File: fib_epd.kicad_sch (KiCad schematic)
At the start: 0 parts

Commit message: restructured EPD side of things, replaced rp2040 with esp32 s3 because of it's LCD controller, USB, LP WIFI_BT & EPDiy compat, repurposed USB0 for ESP interfacing, added e-ink pmic
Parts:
- added U1: TPS651851RSLT, Fibel2:IC_TPS651851, symbol Fibel2:TPS651851RSLT
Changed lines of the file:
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@@
 	(generator_version "8.0")
 	(paper "A4")
+	(symbol
+		(lib_id "Fibel2:TPS651851RSLT")
+		(at 72.39 124.46 0)
+		(unit 1)
+		(exclude_from_sim no)
+		(in_bom yes)
+		(on_board yes)
+		(dnp no)
+		(fields_autoplaced yes)
+		(property "Reference" "U1"
+			(at 72.39 30.48 0)
+			(effects
+				(font
+					(size 1.27 1.27)
+				)
+			)
+		)
+		(property "Value" "TPS651851RSLT"
+			(at 72.39 33.02 0)
+			(effects
+				(font
+					(size 1.27 1.27)
+				)
+			)
+		)
+		(property "Footprint" "Fibel2:IC_TPS651851"
+			(at 73.66 223.266 0)
+			(effects
+				(font
+					(size 1.27 1.27)
+				)
+				(justify bottom)
+				(hide yes)
+			)
+		)
+		(property "Datasheet" ""
+			(at 72.39 124.46 0)
+			(effects
+				(font
+					(size 1.27 1.27)
+				)
+				(hide yes)
+			)
+		)
+		(property "Description" ""
+			(at 72.39 124.46 0)
+			(effects
+				(font
+					(size 1.27 1.27)
+				)
+				(hide yes)
+			)
+		)
+		(property "Package" "VQFN(48)-49 Texas Instruments"
+			(at 73.66 223.266 0)
+			(effects
+				(font
+					(size 1.27 1.27)
+				)
+				(justify bottom)
+				(hide yes)
+			)
+		)
+		(property "MP" "TPS651851RSLT"
+			(at 72.39 124.46 0)
+			(effects
+				(font
+					(size 1.27 1.27)
+				)
+				(justify bottom)
+				(hide yes)
+			)
+		)
+		(pin "5"
+		)
+		(pin "9"
+		)
+		(pin "48"
+		)
+		(pin "19"
+		)
+		(pin "20"
+		)
+		(pin "25"
+		)
+		(pin "16"
+		)
+		(pin "30"
+		)
+		(pin "14"
+		)
+		(pin "24"
+		)
+		(pin "43"
+		)
+		(pin "40"
+		)
+		(pin "12"
+		)
+		(pin "7"
+		)
+		(pin "8"
+		)
+		(pin "10"
+		)
+		(pin "15"
+		)
+		(pin "3"
+		)
+		(pin "18"
+		)
+		(pin "47"
+		)
+		(pin "6"
+		)
+		(pin "39"
+		)
+		(pin "35"
+		)
+		(pin "46"
+		)
+		(pin "36"
+		)
+		(pin "32"
+		)
+		(pin "31"
+		)
+		(pin "27"
+		)
+		(pin "29"
+		)
+		(pin "41"
+		)
+		(pin "13"
+		)
+		(pin "11"
+		)
+		(pin "28"
+		)
+		(pin "38"
+		)
+		(pin "34"
+		)
+		(pin "26"
+		)
+		(pin "4"
+		)
+		(pin "42"
+		)
+		(pin "44"
+		)
+		(pin "45"
+		)
+		(pin "37"
+		)
+		(pin "22"
+		)
+		(pin "17"
+		)
+		(pin "2"
+		)
+		(pin "33"
+		)
+		(pin "1"
+		)
+		(pin "21"
+		)
+		(pin "23"
+		)
+		(instances
+			(project "Fibel2"
+				(path "/862c21e2-7ec9-4f80-a33c-aad02ea9423e/5a179277-42b3-47ed-bc0e-bf53dbccdf92"
+					(reference "U1")
+					(unit 1)
+				)
+			)
+		)
+	)
 )

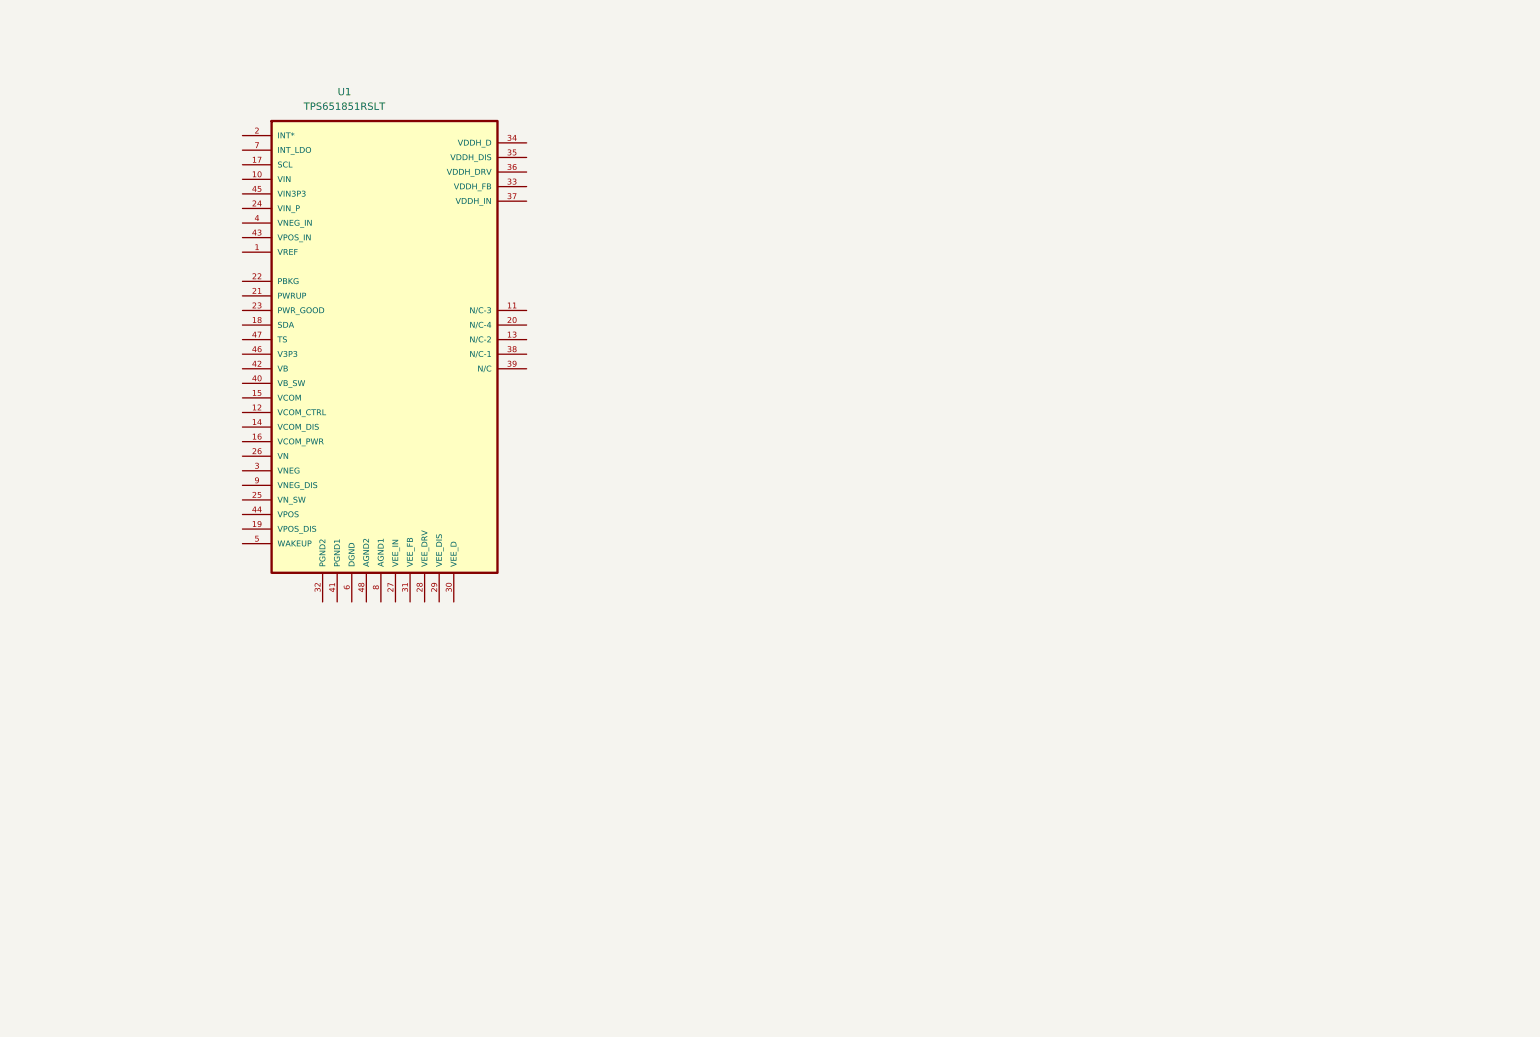
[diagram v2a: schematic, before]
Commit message: partially implemented E-INK PMIC
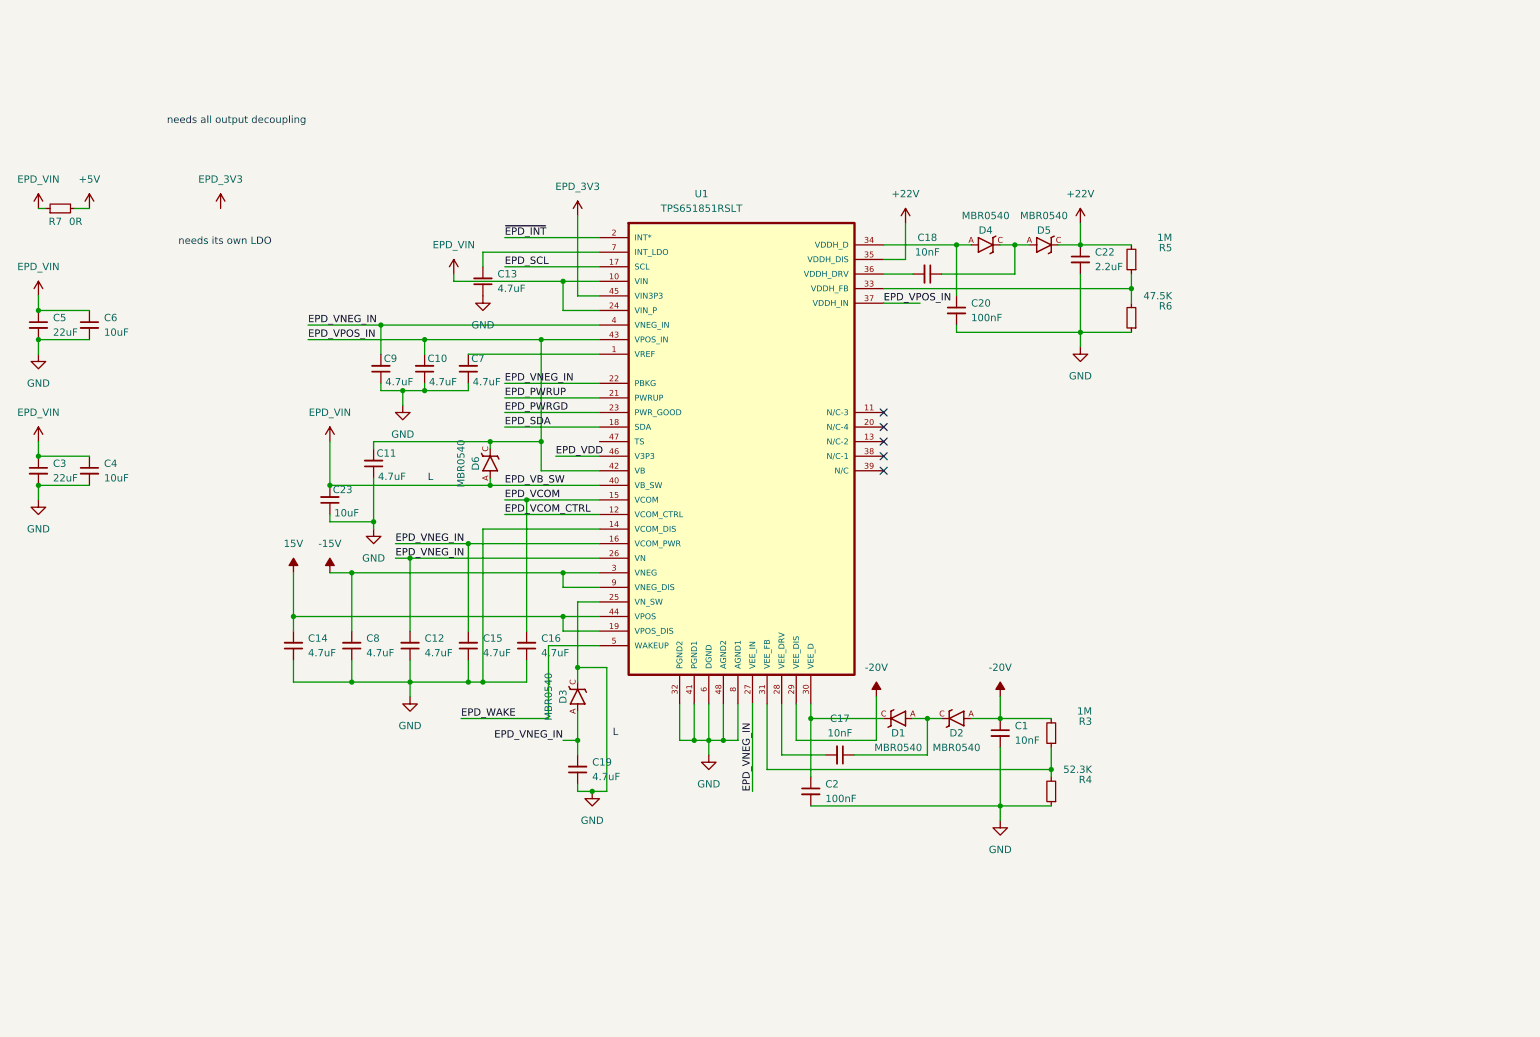
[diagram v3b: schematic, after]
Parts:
- added C1, C17, C18: 10nF, Capacitor_SMD:C_0805_2012Metric, symbol Device:C_Small
- added C10, C11, C12, C13, C14, C15, C16, C19, C7, C8, C9: 4.7uF, Capacitor_SMD:C_0805_2012Metric, symbol Device:C_Small
- added C2, C20: 100nF, Capacitor_SMD:C_0805_2012Metric, symbol Device:C_Small
- added C22: 2.2uF, Capacitor_SMD:C_0805_2012Metric, symbol Device:C_Small
- added C23: 10uF, Capacitor_SMD:C_0805_2012Metric, symbol Device:C_Small
- added C3, C5: 22uF, Capacitor_SMD:C_0805_2012Metric, symbol Device:C_Small
- added C4, C6: 10uF, Capacitor_SMD:C_0603_1608Metric, symbol Device:C_Small
- added D1, D2, D3, D4, D5, D6: MBR0540, MBR0540:SOD-123, symbol Fibel2:MBR0540
- added R3, R5: 1M, Resistor_SMD:R_0603_1608Metric, symbol Device:R_Small
- added R4: 52.3K, Resistor_SMD:R_0603_1608Metric, symbol Device:R_Small
- added R6: 47.5K, Resistor_SMD:R_0603_1608Metric, symbol Device:R_Small
- added R7: 0R, Resistor_SMD:R_0603_1608Metric, symbol Device:R_Small
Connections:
- net at U1.1 (VREF): now also C7.2
- net EPD_VIN: now reaches U1.10 (VIN)
- net EPD_VIN: now also U1.24 (VIN_P), U1.40 (VB_SW), C23.2, C3.1, C4.1, C5.1, C6.1, D6.A, R7.1
- net EPD_VCOM_CTRL: now reaches U1.12 (VCOM_CTRL)
- net GND: now reaches U1.14 (VCOM_DIS)
- net GND: now also U1.25 (VN_SW), U1.32 (PGND2), U1.41 (PGND1), U1.48 (AGND2), U1.6 (DGND), U1.8 (AGND1), C1.2, C10.1, C11.1, C12.1, C13.1, C14.1, C15.1, C16.1, C19.1, C2.2, C20.2, C22.2, C23.1, C3.2, C4.2, C5.2, C6.2, C7.1, C8.1, C9.1, D3.C, R4.1, R6.1
- net EPD_VCOM: now reaches U1.15 (VCOM)
- net EPD_VCOM: now also C16.2
- net EPD_VNEG_IN: now reaches U1.16 (VCOM_PWR)
- net EPD_VNEG_IN: now also U1.22 (PBKG), U1.26 (VN), U1.27 (VEE_IN), U1.4 (VNEG_IN), C12.2, C15.2, C19.2, C9.2, D3.A
- net EPD_SCL: now reaches U1.17 (SCL)
- net EPD_SDA: now reaches U1.18 (SDA)
- net 15V: now reaches U1.19 (VPOS_DIS)
- net 15V: now also U1.44 (VPOS), C14.2
- net ~{EPD_INT}: now reaches U1.2 (INT*)
- net EPD_PWRUP: now reaches U1.21 (PWRUP)
- net EPD_PWRGD: now reaches U1.23 (PWR_GOOD)
- net at U1.28 (VEE_DRV): now also C17.2
- net -20V: now reaches U1.29 (VEE_DIS)
- net -20V: now also C1.1, D2.A, R3.2
- net -15V: now reaches U1.3 (VNEG)
- net -15V: now also U1.9 (VNEG_DIS), C8.2
- net at U1.30 (VEE_D): now also C2.1, D1.C
- net at U1.31 (VEE_FB): now also R3.1, R4.2
- net at U1.33 (VDDH_FB): now also R5.1, R6.2
- net at U1.34 (VDDH_D): now also C20.1, D4.A
- net +22V: now reaches U1.35 (VDDH_DIS)
- net +22V: now also C22.1, D5.C, R5.2
- net at U1.36 (VDDH_DRV): now also C18.2
- net EPD_VPOS_IN: now reaches U1.37 (VDDH_IN)
- net EPD_VPOS_IN: now also U1.42 (VB), U1.43 (VPOS_IN), C10.2, C11.2, D6.C
- net EPD_3V3: now reaches U1.45 (VIN3P3)
- net EPD_VDD: now reaches U1.46 (V3P3)
- net EPD_WAKE: now reaches U1.5 (WAKEUP)
- net at U1.7 (INT_LDO): now also C13.2
- new net: C17.1, D1.A, D2.C
- new net: C18.1, D4.C, D5.A
- new net +5V: R7.2
- no-connect marks 0 -> 5
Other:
- note added: "L"
- note added: "needs all output decoupling"
- note added: "needs its own LDO"
- moved on the sheet: U1

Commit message: added decoupling and inductors for EPD PMIC
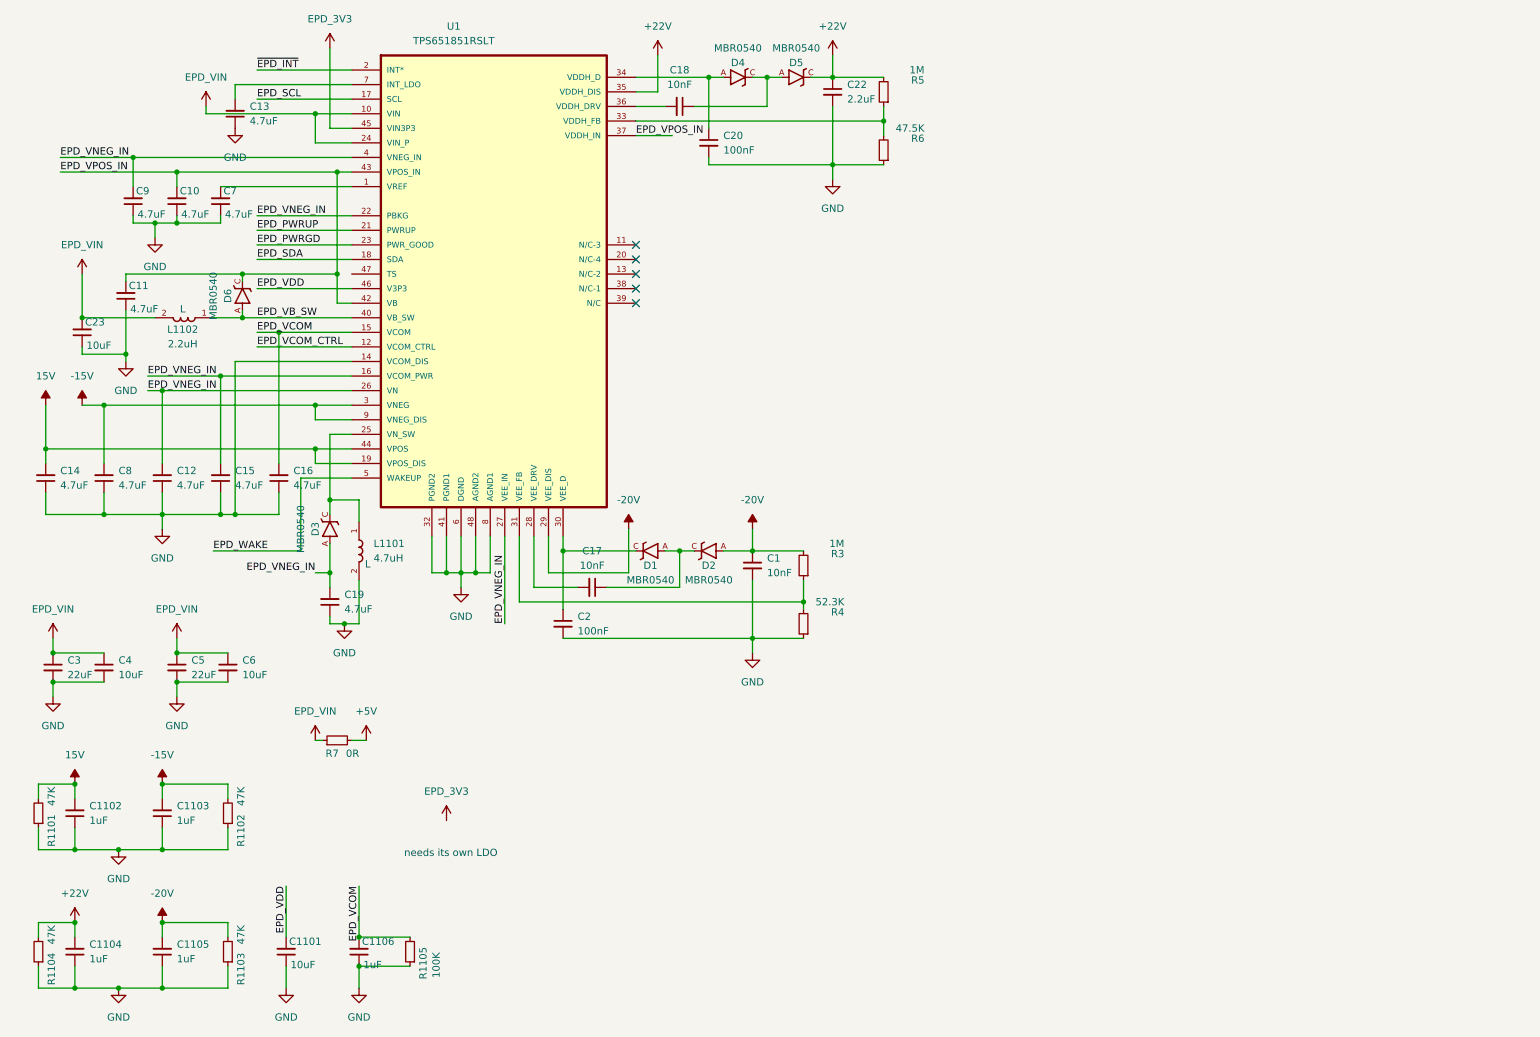
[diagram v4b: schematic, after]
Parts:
- added C1101: 10uF, Capacitor_SMD:C_0805_2012Metric, symbol Device:C_Small
- added C1102, C1103, C1104, C1105, C1106: 1uF, Capacitor_SMD:C_0805_2012Metric, symbol Device:C_Small
- added L1101: 4.7uH, Fibel2:IND_LQH5BPB4R7NT0L, symbol Fibel2:LQH5BPB4R7NT0L
- added L1102: 2.2uH, Fibel2:IND_LQH44PN4R7MP0L, symbol Fibel2:LQH44PN4R7MP0L
- added R1101, R1102, R1103, R1104: 47K, Resistor_SMD:R_0603_1608Metric, symbol Device:R_Small
- added R1105: 100K, Resistor_SMD:R_0603_1608Metric, symbol Device:R_Small
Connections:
- net +22V: now also C1104.2, R1104.2
- net -15V: now also C1103.2, R1102.2
- net -20V: now also C1105.2, R1103.2
- net 15V: now also C1102.2, R1101.2
- net EPD_VCOM: now also C1106.2, R1105.2
- net EPD_VDD: now also C1101.2
- net EPD_VIN: now also L1102.2; no longer D6.A, U1.40 (VB_SW)
- net GND: now also C1101.1, C1102.1, C1103.1, C1104.1, C1105.1, C1106.1, L1101.2, R1101.1, R1102.1, R1103.1, R1104.1, R1105.1; no longer D3.C, U1.25 (VN_SW)
- new net: D3.C, L1101.1, U1.25 (VN_SW)
- new net EPD_VB_SW: D6.A, L1102.1, U1.40 (VB_SW)
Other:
- note removed: "needs all output decoupling"
- moved on the sheet: C1, C10, C11, C12, C13, C14, C15, C16, C17, C18, C19, C2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

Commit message: added connections to ESP32 S3, most oof EPD stuff that we're gooing to use is included
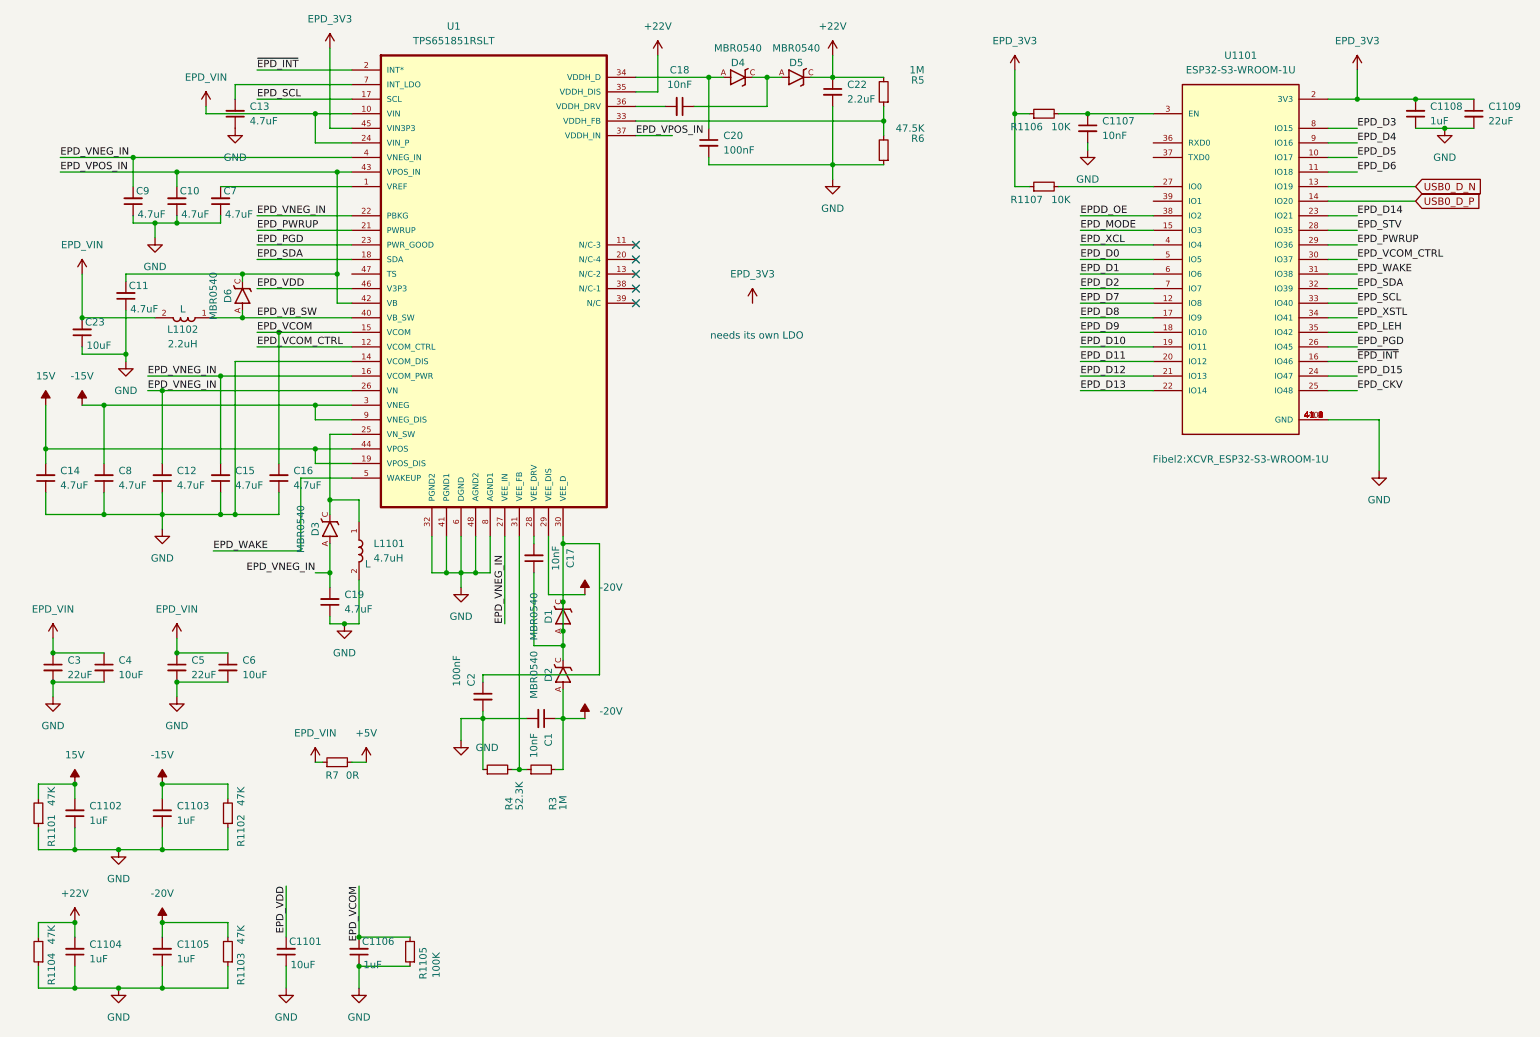
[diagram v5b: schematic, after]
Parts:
- added C1107: 10nF, Capacitor_SMD:C_0805_2012Metric, symbol Device:C_Small
- added C1108: 1uF, Capacitor_SMD:C_0805_2012Metric, symbol Device:C_Small
- added C1109: 22uF, Capacitor_SMD:C_0805_2012Metric, symbol Device:C_Small
- added R1106, R1107: 10K, Resistor_SMD:R_0603_1608Metric, symbol Device:R_Small
- added U1101: ESP32-S3-WROOM-1U, Fibel2:XCVR_ESP32-S3-WROOM-1U, symbol Fibel2:ESP32-S3-WROOM-1U
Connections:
- net EPD_3V3: now also C1108.2, C1109.1, R1106.1, R1107.1, U1101.2 (3V3)
- net EPD_PWRUP: now also U1101.29 (IO36)
- net EPD_SCL: now also U1101.33 (IO40)
- net EPD_SDA: now also U1101.32 (IO39)
- net EPD_VCOM_CTRL: now also U1101.30 (IO37)
- net EPD_WAKE: now also U1101.31 (IO38)
- net GND: now also C1107.2, C1108.1, C1109.2, U1101.1 (GND), U1101.40 (GND), U1101.41_1 (GND), U1101.41_2 (GND), U1101.41_3 (GND), U1101.41_4 (GND), U1101.41_5 (GND), U1101.41_6 (GND), U1101.41_7 (GND), U1101.41_8 (GND), U1101.41_9 (GND)
- net ~{EPD_INT}: now also U1101.16 (IO46)
- net at C17.1, D1.A, D2.C: now also C2.1, D1.C, U1.30 (VEE_D)
- net EPD_PWRGD renamed EPD_PGD
- net EPD_PGD: now also U1101.26 (IO45)
- new net: R1107.2, U1101.27 (IO0)
- new net: C1107.1, R1106.2, U1101.3 (EN)
- new net EPDD_OE: U1101.38 (IO2)
- new net EPD_CKV: U1101.25 (IO48)
- new net EPD_D0: U1101.5 (IO5)
- new net EPD_D1: U1101.6 (IO6)
- new net EPD_D10: U1101.19 (IO11)
- new net EPD_D11: U1101.20 (IO12)
- new net EPD_D12: U1101.21 (IO13)
- new net EPD_D13: U1101.22 (IO14)
- new net EPD_D14: U1101.23 (IO21)
- new net EPD_D15: U1101.24 (IO47)
- new net EPD_D2: U1101.7 (IO7)
- new net EPD_D3: U1101.8 (IO15)
- new net EPD_D4: U1101.9 (IO16)
- new net EPD_D5: U1101.10 (IO17)
- new net EPD_D6: U1101.11 (IO18)
- new net EPD_D7: U1101.12 (IO8)
- new net EPD_D8: U1101.17 (IO9)
- new net EPD_D9: U1101.18 (IO10)
- new net EPD_LEH: U1101.35 (IO42)
- new net EPD_MODE: U1101.15 (IO3)
- new net EPD_STV: U1101.28 (IO35)
- new net EPD_XCL: U1101.4 (IO4)
- new net EPD_XSTL: U1101.34 (IO41)
- new net USB0_D_N: U1101.13 (IO19)
- new net USB0_D_P: U1101.14 (IO20)
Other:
- moved on the sheet: C1, C17, C2, D1, D2, R3, R4, R7
